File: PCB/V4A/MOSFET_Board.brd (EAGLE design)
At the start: 100 x 100 mm, 72 parts, among them IC101 7805T, Q101 IXTK102N65X2, Q102 BC817-16SMD, Q103 SIRC10DP, Q104 SIRC10DP, Q105 BC817-16SMD, Q106 BC807-16SMD, U101 AD620, U102 AD620, U103 LTC1865L, U104 LT1014I, U105 AD420, U106 LP2985-3.1, X201 SMKDSP_1,5/2, X202 SMKDSP_1,5/2

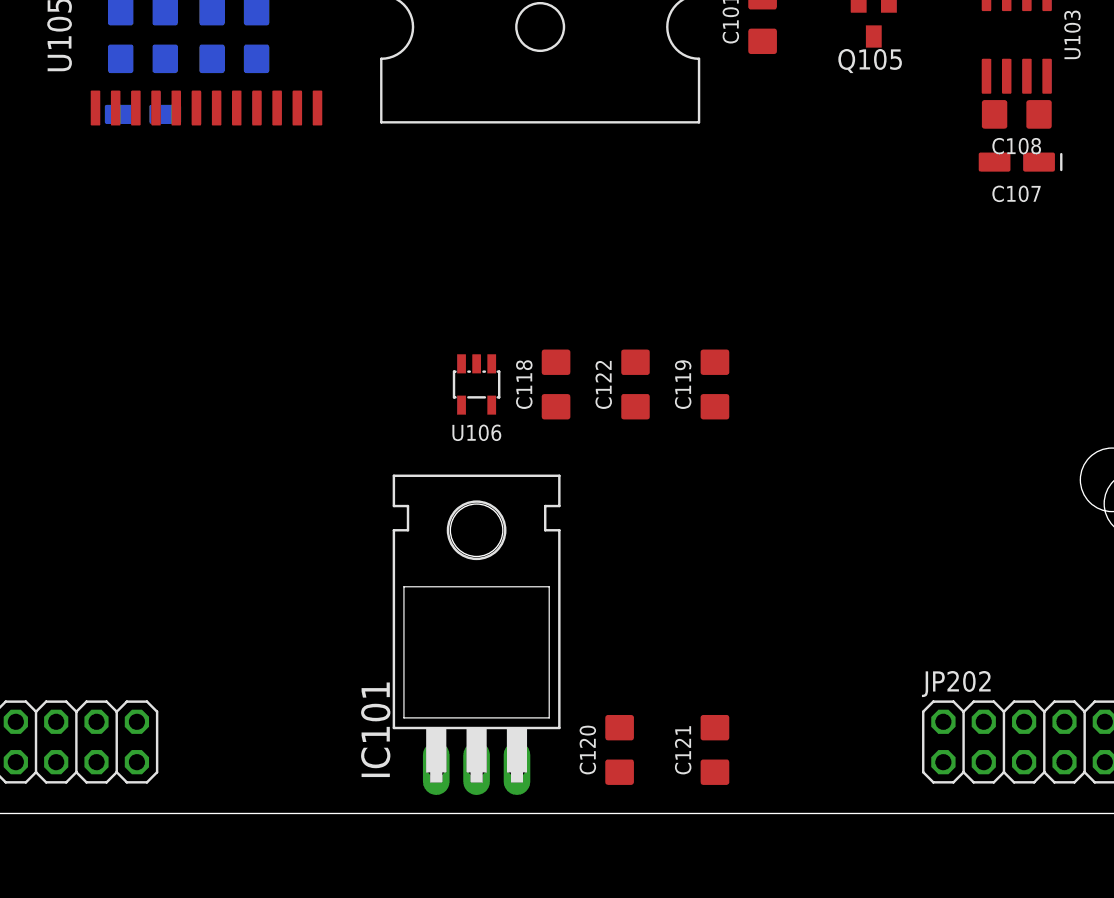
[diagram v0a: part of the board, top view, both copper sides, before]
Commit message: Added optoisolation to MOSFET board
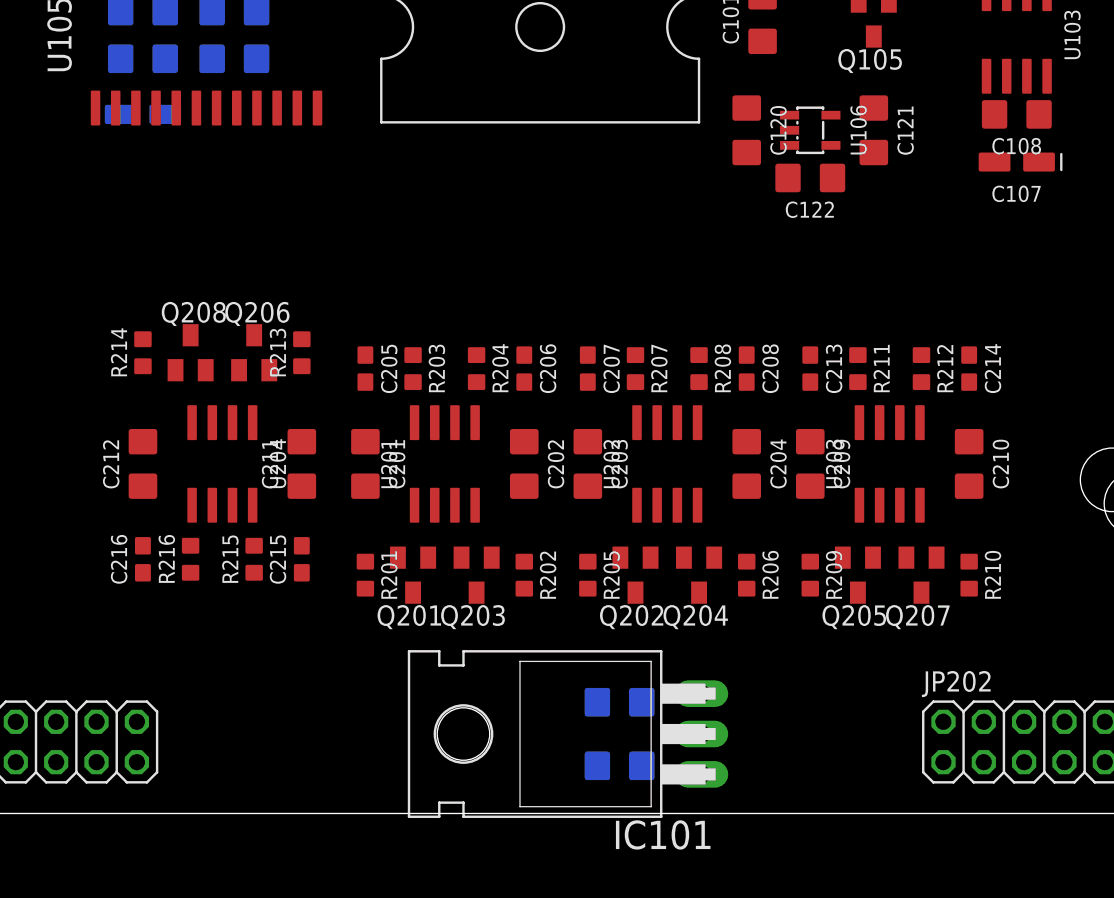
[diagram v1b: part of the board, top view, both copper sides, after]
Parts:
- added C201, C203, C209, C211: 0.1µ, passives:C3216
- added C202, C204, C210, C212: 0.01µ, passives:C3216
- added C205, C206, C207, C208, C213, C214, C215, C216: 15p, passives:C1608
- added Q201, Q202, Q203, Q204, Q205, Q206, Q207, Q208: BC807-16SMD, transistor-pnp:SOT23-BEC
- added R201, R202, R203, R204, R205, R206, R207, R208, R209, R210, R211, R212, R213, R214, R215, R216: 350R, passives:R1608
- added U201, U202, U203, U204: HCPL-063N, ic:SO8
- C118: value 1µ -> 0.33µ
- C119: value 2µ2 -> 0.1µ
- C120: value 0.33µ -> 1µ
- C121: value 0.1µ -> 2µ2
- moved C121 40.3 mm to (21.0, -14.0), turned to 270 degrees
- moved C120 39.8 mm to (13.0, -14.0), turned to 270 degrees
- moved U106 26.4 mm to (17.0, -14.0), turned to 270 degrees
- moved C118 24.3 mm to (5.00, -54.0), flipped to the bottom, turned to 0 degrees
- moved C119 20.9 mm to (5.00, -50.0), flipped to the bottom, turned to 0 degrees
- moved C122 17.0 mm to (17.0, -17.0), turned to 180 degrees
- moved IC101 8.94 mm to (0.00, -52.0), turned to 90 degrees
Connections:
- new net BYP_ISO: C102.1, C213.1, R106.1, R211.1, U203.7
- new net CLR_DAC_ISO: C205.1, R203.1, U105.6, U201.7
- new net FLT_DAC_ISO: Q208.B, U105.3
- new net MISO_ISO: Q206.B, U103.6
- new net MOSI_ISO: C208.1, R208.1, U103.5, U105.9, U202.6
- new net N$17: Q206.E, R213.1, U204.1
- new net N$18: Q208.E, R214.1, U204.4
- new net N$19: Q202.E, R205.1, U202.1
- new net N$20: Q204.E, R206.1, U202.4
- new net N$21: Q205.E, R209.1, U203.1
- new net N$22: Q207.E, R210.1, U203.4
- new net N$23: JP201.7
- new net N$24: JP201.5
- new net N$26: JP202.1
- new net N$27: JP201.9
- new net N$28: JP201.11
- new net N$29: JP201.13
- new net N$30: JP202.2
- new net N$32: JP201.6
- new net N$33: JP201.8
- new net N$34: JP201.10
- new net N$35: JP201.12
- new net N$36: JP201.14
- new net N$37: JP202.3
- new net N$38: JP202.5
- new net N$39: JP202.7
- new net N$40: JP202.9
- new net N$45: JP202.10
- new net N$46: JP202.8
- new net N$47: JP202.6
- new net N$48: JP202.4
- new net N$76: Q201.E, R201.1, U201.1
- new net N$77: Q203.E, R202.1, U201.4
- new net SCK_ISO: C207.1, R207.1, U103.7, U105.8, U202.7
- new net SS_C_ISO: C214.1, R212.1, U103.1, U203.6
- new net SS_DAC_ISO: C206.1, R204.1, U105.7, U201.6
- net +12V: now also C118.1, JP201.3, JP202.11; no longer C120.1
- net +15V: now also JP201.1, JP202.13
- net +3V3: now also C121.1, R207.2, R208.2, R212.2; no longer C119.1
- net +5V: now also C119.1, C201.1, C202.1, C203.1, C204.1, C209.1, C210.1, C211.1, C212.1, R201.2, R202.2, R203.2, R204.2, R205.2, R206.2, R209.2, R210.2, R211.2, R213.2, R214.2, R215.2, R216.2, U201.8, U202.8, U203.8, U204.8; no longer C121.1
- net -15V: now also JP201.2, JP202.14
- net BYP: now also Q205.B; no longer C102.1, R106.1
- net CLR_DAC: now also Q201.B; no longer U105.6
- net FLT_DAC: now also C216.1, R216.1, U204.6; no longer U105.3
- net GND: now also C201.2, C202.2, C203.2, C204.2, C205.2, C206.2, C207.2, C208.2, C209.2, C210.2, C211.2, C212.2, C213.2, C214.2, C215.2, C216.2, JP201.4, JP202.12, Q201.C, Q202.C, Q203.C, Q204.C, Q205.C, Q206.C, Q207.C, Q208.C, U201.2, U201.3, U201.5, U202.2, U202.3, U202.5, U203.2, U203.3, U203.5, U204.2, U204.3, U204.5
- net MISO: now also C215.1, R215.1, U204.7; no longer U103.6
- net MOSI: now also Q204.B; no longer U103.5, U105.9
- net SCK: now also Q202.B; no longer U103.7, U105.8
- net SS_C: now also Q207.B; no longer U103.1
- net SS_DAC: now also Q203.B; no longer U105.7
- net VREF: now also C120.1; no longer C118.1

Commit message: Changed to single board design
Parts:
- removed C201, C203, C209, C211: 0.1µ, passives:C3216
- removed C202, C204, C210, C212: 0.01µ, passives:C3216
- removed C205, C206, C207, C208, C213, C214, C215, C216: 15p, passives:C1608
- removed Q201, Q202, Q203, Q204, Q205, Q206, Q207, Q208: BC807-16SMD, transistor-pnp:SOT23-BEC
- removed R201, R202, R203, R204, R205, R206, R207, R208, R209, R210, R211, R212, R213, R214, R215, R216: 350R, passives:R1608
- removed U$2, U$3, U$4, U$5: (no value), mechanical:M3
- removed U201, U202, U203, U204: HCPL-063N, ic:SO8
- removed X201, X202: SMKDSP_1,5/2, con-phoenix-smkdsp:SMKDSP_1,5/2
- added C123, C124, C131, C132, C134, C301, C302, C309, C310: 0.1µ, passives:C3216
- added C125, C126, C127, C128: 100p, passives:C1608
- added C129, C130: 1µ, passives:CT3216
- added C133: 0.33µ, passives:C3216
- added C135: 1µ, passives:C3216
- added C136: 10n, passives:C3216
- added C137: 2µ2, passives:C3216
- added C303, C304, C311, C312: 0.01µ, passives:C3216
- added C305, C306, C307, C308, C313, C314, C315, C316: 15p, passives:C1608
- added D101, D102, D103, D104: BAT54S, diode:SOT23
- added HS102: (no value), mechanical:HEATSINK-LGA115X
- added LCD1: LCD-20X4, mechanical:4X20_LED
- added PS101: RFMM-0505S, modules:RECOM-SIP7
- added Q107, Q109: BC817, transistors:SOT23
- added Q108, Q110, Q301, Q302, Q303, Q304, Q305, Q306, Q307, Q308: BC807, transistors:SOT23
- added Q111, Q112: IXTK102N65X2, transistors:TO-264P-H-PADUP
- added R129, R130: 100R, passives:R3216W
- added R131, R133, R137, R139: 1k, passives:R1608
- added R132, R134, R138, R140, R143, R144: 2R, passives:R3216W
- added R135, R136: 100k, passives:R1608
- added R141, R142, R146, R148: 0R004, passives:R6332W
- added R145, R147, R149, R150, R151, R152: 2k15, passives:R2012W
- added R153, R154, R155, R156: 100R, passives:R2012W
- added R301, R302, R303, R304, R305, R306, R307, R308, R309, R310, R311, R312, R313, R314, R315, R316: 350R, passives:R1608
- added U$1: ARDUINO-MICRO, breakout:ARDUINO-MICRO
- added U107, U108: AD620, ic:SO8
- added U109, U110: LTC1865L, ic:SO8
- added U111: LP2985-3.1, ic:SOT23-5L
- added U301, U302, U303, U304: HCPL-063N, ic:SO8
- added X301, X302, X303, X304: SMKDSP_1,5/2, con-phoenix-smkdsp:SMKDSP_1,5/2
- C102: value 500p -> 0.1µ; device passives:C1608 -> passives:C3216
- C105, C106, C108: value 0.1µ -> 0.01µ
- C107: value 1µ -> 0.01µ; device passives:CT3216 -> passives:C3216
- C109, C110: value 500p -> 1µ; device passives:C1608 -> passives:CT3216
- C113, C114: value 0.01µ -> 0.1µ
- C115: value 1µ -> 0.1µ; device passives:CT3216 -> passives:C3216
- C118: value 0.33µ -> 0.1µ
- C120: value 1µ -> 0.1µ
- C121: value 2µ2 -> 0.1µ
- C122: value 10n -> 0.1µ
- HS101: value HEATSINK-LGA115X -> (none)
- Q101: value IXTK102N65X2 -> SIRC10DP; device transistors:TO-264P-H-PADUP -> transistors:POWERPAK-SO-8
- Q102, Q105: value BC817-16SMD -> SIRC10DP; device transistor-npn:SOT23-BEC -> transistors:POWERPAK-SO-8
- Q103, Q104: value SIRC10DP -> BC817; device transistors:POWERPAK-SO-8 -> transistors:SOT23
- Q106: value BC807-16SMD -> SIRC10DP; device transistor-pnp:SOT23-BEC -> transistors:POWERPAK-SO-8
- R101, R117: value 100k -> 10k
- R102: value 1k -> 10k
- R103, R104, R107: value 2R -> 10k; device passives:R3216W -> passives:R1608
- R105: value 2k15 -> 100k; device passives:R2012W -> passives:R1608
- R106: value 1k -> 100k
- R108, R109: value 0R004 -> 10k; device passives:R6332W -> passives:R1608
- R110, R111, R126: value 2k15 -> 10k; device passives:R2012W -> passives:R1608
- R112, R113: value 100R -> 10k; device passives:R2012W -> passives:R1608
- R123: value 100R -> 10k; device passives:R3216W -> passives:R1608
- R127, R128: value 10k -> 2k15; device passives:R1608 -> passives:R2012W
- U101, U102: value AD620 -> AD420; device ic:SO8 -> ic:SO24W
- U103: value LTC1865L -> LT1014I; device ic:SO8 -> ic:SO16W
- U105: value AD420 -> AD620; device ic:SO24W -> ic:SO8
- U106: value LP2985-3.1 -> AD620; device ic:SOT23-5L -> ic:SO8
- moved R108 342.6 mm to (-60.0, -304.0), turned to 0 degrees
- moved C120 330.0 mm to (-75.0, -332.0), turned to 0 degrees
- moved R110 329.1 mm to (-68.0, -304.0), turned to 0 degrees
- moved R104 323.5 mm to (-72.0, -304.0), turned to 0 degrees
- moved R112 320.4 mm to (-56.0, -304.0), turned to 0 degrees
- moved C104 317.5 mm to (-55.0, -293.0), turned to 0 degrees
- moved R106 316.9 mm to (-75.0, -299.0), turned to 0 degrees
- moved R124 312.8 mm to (-63.0, -299.0), flipped to the top, turned to 0 degrees
- moved R126 312.6 mm to (-67.0, -299.0), flipped to the top, turned to 0 degrees
- moved R120 312.0 mm to (-59.0, -299.0), flipped to the top, turned to 0 degrees
- moved C112 311.4 mm to (-70.0, -293.0), flipped to the top, turned to 0 degrees
- moved R118 311.4 mm to (-76.0, -304.0), flipped to the top, turned to 0 degrees
- moved C102 310.7 mm to (-60.0, -293.0), turned to 0 degrees
- moved R122 310.6 mm to (-71.0, -299.0), flipped to the top, turned to 0 degrees
- moved R117 310.0 mm to (-64.0, -304.0), flipped to the top, turned to 0 degrees
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- renumbered JP201 to JP301, JP202 to JP302
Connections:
- removed net BYP_GATE: Q102.E, Q106.E, R104.1, R105.2, R107.1
- removed net CSENSE_H: Q103.1, Q103.2, Q103.3, Q104.1, Q104.2, Q104.3, R103.1, R105.1, R108.2, R109.2, U101.3, U102.2
- removed net CSENSE_L: Q101.1, Q103.5, Q104.5, R103.2, R125.1, R126.1, U102.3
- removed net HIGHC: C109.1, R112.2, U103.2
- removed net LBQ12_G: Q103.4, R104.2
- removed net LBQ13_G: Q104.4, R107.2
- removed net LGATE: Q101.3, R123.2
- removed net LOWC: C110.1, R113.2, U103.3
- removed net SDO_DAC: U105.10
- new net +VI: PS101.1
- new net +VO: PS101.7
- new net -VI: PS101.2
- new net -VO: PS101.5
- new net 3.3V: U$1.19
- new net A: LCD1.15
- new net BPY1G1: Q101.4, R132.2
- new net BYP1: Q109.2, Q110.2, R132.1, R138.1, R147.1
- new net BYP1G2: Q105.4, R138.2
- new net BYP2: Q107.2, Q108.2, R134.1, R140.1, R145.2
- new net BYP2G1: Q102.4, R134.2
- new net BYP2G2: Q106.4, R140.2
- new net CLR_DAC1: U101.6
- new net CLR_DAC2: U102.6
- new net CONV_C1: U109.1
- new net CONV_C2: U110.1
- new net CSEN_H1: Q101.1, Q101.2, Q101.3, Q105.1, Q105.2, Q105.3, R141.2, R143.1, R146.2, R147.2, U105.3, U106.2
- new net CSEN_H2: Q102.1, Q102.2, Q102.3, Q106.1, Q106.2, Q106.3, R142.2, R144.1, R145.1, R148.2, U107.3, U108.2
- new net CSEN_L1: Q101.5, Q105.5, Q111.1, R101.1, R127.1, R143.2, U106.3
- new net CSEN_L2: Q102.5, Q106.5, Q112.1, R102.1, R128.1, R144.2, U108.3
- new net DAC_VOUT1: U102.17, U104.5
- new net HIGHC1: C125.1, R153.2, U109.2
- new net HIGHC2: C127.1, R155.2, U110.2
- new net K: LCD1.16
- new net LATCH_DAC: U101.7, U102.7
- new net LGATE_1: Q111.3, R129.2
- new net LGATE_2: Q112.3, R130.2
- new net LOWC1: C126.1, R154.2, U109.3
- new net LOWC2: C128.1, R156.2, U110.3
- new net N$15: U103.1, U103.2
- new net N$25: Q103.3, Q107.1, Q108.1, R137.1
- new net N$31: Q103.1, R131.2, R135.1
- new net N$41: C106.2, U102.21
- new net N$42: C108.2, U102.20
- new net N$43: R106.2, R108.2, R112.2, R116.1, R117.1, U104.6
- new net N$44: R118.2, R122.1, U104.10
- new net N$49: R102.2, R118.1, U104.11
- new net N$50: R104.2, R110.2, U104.12
- new net N$51: R122.2, R126.1, U104.15
- new net N$52: R126.2, R128.2, R130.1, U104.16
- new net N$53: R120.2, R124.2, U104.14
- new net N$54: R116.2, R117.2, R120.1, U104.7
- new net N$56: D103.3, R155.1, U107.6
- new net N$57: D104.3, R156.1, U108.6
- new net RG1_L1: R151.2, U107.1
- new net RG1_L2: R152.2, U108.1
- new net RG2_L1: R151.1, U107.8
- new net RG2_L2: R152.1, U108.8
- new net SDO_DAC1: U101.10, U102.9
- new net SDO_DAC2: U102.10
- new net VDD: LCD1.2
- new net VEE: LCD1.3
- new net VIN: U$1.32
- new net VSS: LCD1.1
- net +12V: now also C105.1, C106.1, C107.1, C108.1, C115.1, C116.1, C133.1, Q107.3, Q109.3, R135.2, R136.2, R137.2, R139.2, U101.23, U102.23; no longer C101.1, C117.1, C118.1, Q102.C, R101.2, R102.2, U105.23
- net +15V: now also C101.1, C102.1, C117.1, C118.1, C119.1, C120.1, U103.4, U105.7, U106.7, U107.7, U108.7; no longer C103.1, C105.1, C111.1, U101.7, U102.7
- net +3V3: now also C129.+, C130.+, C131.1, C132.1, C137.1, D101.2, D102.2, D103.2, D104.2, R308.2, R313.2, R314.2, U109.8, U110.8, U111.5; no longer C107.+, C108.1, C121.1, R207.2, R208.2, R212.2, U103.8, U106.5
- net +5V: now also C109.+, C110.+, C111.1, C112.1, C134.1, C301.1, C302.1, C303.1, C304.1, C309.1, C310.1, C311.1, C312.1, R301.2, R302.2, R303.2, R304.2, R305.2, R306.2, R307.2, R309.2, R310.2, R311.2, R312.2, R315.2, R316.2, U$1.29, U101.2, U102.2, U301.8, U302.8, U303.8, U304.8; no longer C115.+, C116.1, C119.1, C201.1, C202.1, C203.1, C204.1, C209.1, C210.1, C211.1, C212.1, R201.2, R202.2, R203.2, R204.2, R205.2, R206.2, R209.2, R210.2, R211.2, R213.2, R214.2, R215.2, R216.2, U105.2, U201.8, U202.8, U203.8, U204.8
- net -15V: now also C103.1, C121.1, C122.1, C123.1, C124.1, U103.13, U105.4, U106.4, U107.4, U108.4; no longer C106.1, C112.1, U101.4, U102.4
- net BYP: now also Q302.1; no longer Q205.B
- net BYP_ISO: now also C306.1, R131.1, R133.1, R306.1, U302.7; no longer C102.1, C213.1, R106.1, R211.1, U203.7
- net CLR_DAC: now also Q301.1; no longer Q201.B
- net CLR_DAC_ISO: now also C305.1, R305.1, U301.7; no longer C205.1, R203.1, U105.6, U201.7
- net DAC_VOUT: now also U101.17, U103.5; no longer U104.5, U105.17
- net DUT+: now also Q111.2, Q112.2, X301.1, X301.2; no longer Q101.2, X201.1, X201.2
- net DUT-: now also U105.2, U107.2; no longer U101.2
- net FLT_DAC: now also C316.1, R316.1, U101.3, U102.3, U304.6; no longer C216.1, R216.1, U204.6
- net FLT_DAC_ISO: now also Q308.1; no longer Q208.B, U105.3
- net GND: now also C102.2, C109.-, C110.-, C113.2, C114.2, C115.2, C123.2, C124.2, C125.2, C126.2, C127.2, C128.2, C129.-, C130.-, C131.2, C132.2, C133.2, C134.2, C135.2, C136.2, C137.2, C301.2, C302.2, C303.2, C304.2, C305.2, C306.2, C307.2, C308.2, C309.2, C310.2, C311.2, C312.2, C313.2, C314.2, C315.2, C316.2, D101.1, D102.1, D103.1, D104.1, Q103.2, Q104.2, Q108.3, Q110.3, Q301.3, Q302.3, Q303.3, Q304.3, Q305.3, Q306.3, Q307.3, Q308.3, R103.1, R104.1, R107.1, R110.1, R111.1, R112.1, R123.1, R124.1, R141.1, R142.1, R146.1, R148.1, U$1.31, U$1.6, U101.11, U101.4, U102.11, U102.4, U103.3, U106.5, U107.5, U108.5, U109.4, U110.4, U111.2, U301.2, U301.3, U301.5, U302.2, U302.3, U302.5, U303.2, U303.3, U303.5, U304.2, U304.3, U304.5, X302.1, X302.2; no longer C105.2, C106.2, C107.-, C108.2, C109.2, C110.2, C115.-, C201.2, C202.2, C203.2, C204.2, C205.2, C206.2, C207.2, C208.2, C209.2, C210.2, C211.2, C212.2, C213.2, C214.2, C215.2, C216.2, Q105.E, Q106.C, Q201.C, Q202.C, Q203.C, Q204.C, Q205.C, Q206.C, Q207.C, Q208.C, R118.1, R119.1, R122.1, R127.1, R128.1, U103.4, U105.11, U105.4, U106.2, U201.2, U201.3, U201.5, U202.2, U202.3, U202.5, U203.2, U203.3, U203.5, U204.2, U204.3, U204.5, X202.1, X202.2
- net MISO: now also C315.1, R315.1, U109.6, U110.6, U304.7; no longer C215.1, R215.1, U204.7
- net MISO_ISO: now also Q307.1; no longer Q206.B, U103.6
- net MOSI: now also Q306.1, U101.9, U109.5, U110.5; no longer Q204.B
- net MOSI_ISO: now also C314.1, R314.1, U303.6; no longer C208.1, R208.1, U103.5, U105.9, U202.6
- net N$1: now also R103.2, R109.2, U103.12; no longer R122.2, R127.2, U104.12
- net N$10: now also C136.1, U111.4; no longer C122.1, U106.4
- net N$11: now also R113.2, R119.1, U103.7; no longer R115.2, R116.1, U104.7
- net N$12: now also R105.2, R107.2, R111.2, R113.1, U103.6; no longer R115.1, R117.2, R118.2, R119.2, U104.6
- net N$13: now also R115.2, R121.1, U103.10; no longer R121.2, R124.1, U104.10
- net N$14: now also R101.2, R115.1, U103.11; no longer R121.1, R125.2, U104.11
- net N$16: now also D102.3, R154.1, U106.6; no longer R113.1, U102.6
- net N$17: now also Q307.2, R311.1, U304.1; no longer Q206.E, R213.1, U204.1
- net N$18: now also Q308.2, R312.1, U304.4; no longer Q208.E, R214.1, U204.4
- net N$19: now also Q305.2, R309.1, U303.1; no longer Q202.E, R205.1, U202.1
- net N$2: now also R121.2, R125.1, U103.15; no longer R120.1, R124.2, U104.15
- net N$20: now also Q306.2, R310.1, U303.4; no longer Q204.E, R206.1, U202.4
- net N$21: now also Q302.2, R302.1, U302.1; no longer Q205.E, R209.1, U203.1
- net N$22: now also Q304.2, R304.1, U302.4; no longer Q207.E, R210.1, U203.4
- net N$3: now also C105.2, U101.21; no longer C113.2, U105.21
- net N$4: now also C107.2, U101.20; no longer C114.2, U105.20
- net N$5: now also Q104.3, Q109.1, Q110.1, R139.1; no longer Q102.B, Q105.C, Q106.B, R102.1
- net N$6: now also R125.2, R127.2, R129.1, U103.16; no longer R120.2, R123.1, R126.2, U104.16
- net N$7: now also D101.3, R153.1, U105.6; no longer R112.1, U101.6
- net N$76: now also Q301.2, R301.1, U301.1; no longer Q201.E, R201.1, U201.1
- net N$77: now also Q303.2, R303.1, U301.4; no longer Q203.E, R202.1, U201.4
- net N$8: now also Q104.1, R133.2, R136.1; no longer C102.2, Q105.B, R101.1, R106.2
- net N$9: now also R119.2, R123.2, U103.14; no longer R116.2, R128.2, U104.14
- net RG1_L3: now also R149.2, U105.1; no longer R110.2, U101.1
- net RG1_L4: now also R150.2, U106.1; no longer R111.2, U102.1
- net RG2_L3: now also R149.1, U105.8; no longer R110.1, U101.8
- net RG2_L4: now also R150.1, U106.8; no longer R111.1, U102.8
- net SCK: now also Q305.1, U101.8, U102.8, U109.7, U110.7; no longer Q202.B
- net SCK_ISO: now also C313.1, R313.1, U303.7; no longer C207.1, R207.1, U103.7, U105.8, U202.7
- net SS_C: now also Q304.1; no longer Q207.B
- net SS_C_ISO: now also C308.1, R308.1, U302.6; no longer C214.1, R212.1, U103.1, U203.6
- net SS_DAC: now also Q303.1; no longer Q203.B
- net SS_DAC_ISO: now also C307.1, R307.1, U301.6; no longer C206.1, R204.1, U105.7, U201.6
- net VREF: now also C135.1, R105.1, R106.1, U101.14, U101.15, U102.15, U111.1, U111.3; no longer C120.1, R117.1, U105.14, U105.15, U106.1, U106.3
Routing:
- net N$55: track 1.27 -> 0.00 mm
- net N$15: track 0.00 -> 1.27 mm
- added copper zone on layer 1, net CSEN_H1
- added copper zone on layer 1, net CSEN_L2
- removed copper zone on layer 1, net CSENSE_H
- removed copper zone on layer 1, net CSENSE_L
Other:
- board size 100 x 100 mm -> 200 x 155 mm

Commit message: PCB layout
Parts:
- removed C133: 0.33µ, passives:C3216
- removed C134: 0.1µ, passives:C3216
- removed IC101: 7805T, linear:TO220H
- removed JP301, JP302: (no value), pinhead:2X07
- removed LCD1: LCD-20X4, mechanical:4X20_LED
- removed U$1: ARDUINO-MICRO, breakout:ARDUINO-MICRO
- removed X301, X302, X303, X304: SMKDSP_1,5/2, con-phoenix-smkdsp:SMKDSP_1,5/2
- added C1, C11, C220, C3, C6: 1µ, passives:CT3216
- added C10: 10µ, passives:CT6032
- added C12, C8: 10n, passives:C3216
- added C13: 22µ, passives:CT6032
- added C14, C15: 220µ, rcl:E3,5-10
- added C16, C18: 0.33µ, passives:C3216
- added C17, C19: 0.1µ, passives:C1608
- added C2, C215, C219, C221, C7, C9: 0.1µ, passives:C3216
- added C218, C4, C5: 500p, passives:C1608
- added D301, D302: 1N5817-B, diode:DO41-7.6
- added IC1, IC2: 7805T, linear:TO220H
- added J1: (no value), con-jack:SPC4078
- added JP1: (no value), pinhead:1X16
- added L301, L302: 100µ, passives:SRN1060
- added MOV201, MOV202, MOV203, MOV204: 180V, passives:R3225W
- added R1, R2: 0R01, passives:R6332W
- added R205, R206, R207, R212, R213: 2M, passives:R3216W
- added R214, R215: 2k15, passives:R2012W
- added R216, R3, R4: 100R, passives:R2012W
- added R217: 10k, passives:R1608
- added U$2, U$3: FAN_MOLEX4PIN, mechanical:MOLEX_47053-1000
- added U$6, U$7, U$8, U$9: (no value), mechanical:M4
- added U1, U2: LM50, ic:SOT23W
- added U205: AD620, ic:SO8
- added U208, U3: LTC1865L, ic:SO8
- added U4: MAX743, ic:SO16W
- added X1: GMSTBA4, con-phoenix-762:GMSTBA4
- C101, C102, C103, C104, C111, C112, C113, C114, C115, C116, C117, C118, C119, C120, C121, C122, C123, C124, C131, C132, C301, C302, C309, C310: device passives:C3216 -> passives:C1608
- C105, C107, C136: device passives:C3216 -> passives:C2012
- C137: value 2µ2 -> 4µ7
- R141, R142, R146, R148: value 0R004 -> 0R01
- R143, R144: value 2R -> 3R3
- moved R118 468.5 mm to (163.0, 99.0), turned to 270 degrees
- moved R104 467.0 mm to (169.0, 96.0), turned to 270 degrees
- moved R106 466.8 mm to (169.0, 99.0), turned to 270 degrees
- moved R110 463.4 mm to (166.0, 96.0), turned to 270 degrees
- moved R112 460.1 mm to (166.0, 99.0), turned to 270 degrees
- moved R117 459.9 mm to (163.0, 96.0), turned to 270 degrees
- moved R126 458.2 mm to (160.0, 99.0), turned to 270 degrees
- moved R108 456.8 mm to (166.0, 93.0), turned to 270 degrees
- moved R122 455.0 mm to (160.0, 93.0), turned to 270 degrees
- moved R124 453.6 mm to (160.0, 96.0), turned to 270 degrees
- moved R102 449.5 mm to (169.0, 93.0), turned to 270 degrees
- moved R116 448.5 mm to (163.0, 93.0), turned to 270 degrees
- moved R120 447.6 mm to (157.0, 93.0), turned to 270 degrees
- moved R130 445.9 mm to (170.0, 104.0), turned to 90 degrees
- moved U104 445.7 mm to (163.0, 96.0), flipped to the bottom
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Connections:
- removed net +VI: PS101.1
- removed net +VO: PS101.7
- removed net -VI: PS101.2
- removed net -VO: PS101.5
- removed net 3.3V: U$1.19
- removed net A: LCD1.15
- removed net K: LCD1.16
- removed net N$40: JP302.9
- removed net N$46: JP302.8
- removed net N$47: JP302.6
- removed net N$48: JP302.4
- removed net VDD: LCD1.2
- removed net VEE: LCD1.3
- removed net VIN: U$1.32
- removed net VREF: C135.1, R105.1, R106.1, U101.14, U101.15, U102.15, U111.1, U111.3
- removed net VSS: LCD1.1
- new net +5V_I: C310.1, C312.1, PS101.7
- new net FAN1_PWM: U$2.4
- new net FAN1_SIG: U$2.3
- new net FAN2_PWM: U$3.4
- new net FAN2_SIG: U$3.3
- new net GNDI: C310.2, C312.2, C315.2, C316.2, PS101.5, Q301.3, Q302.3, Q303.3, Q304.3, Q305.3, Q306.3, U301.2, U301.3, U302.2, U302.3, U303.2, U303.3, U304.5
- new net MISO_I: U208.6, U3.6
- new net MOSI_I: U208.5, U3.5
- new net RG1_H6: R215.2, U205.1
- new net RG2_H6: R215.1, U205.8
- new net SCK_I: U208.7, U3.7
- new net SS_TEMP_I: U3.1
- new net SS_V_I: U208.1
- new net T1_OUT: C1.+, R3.1, U1.2
- new net T2_OUT: C3.+, R4.1, U2.2
- new net TEMP1: C4.1, R3.2, U3.2
- new net TEMP2: C5.1, R4.2, U3.3
- new net VREF1: C135.1, R105.1, U101.14, U101.15, U111.1, U111.3
- new net VREF2: C10.+, R106.1, U102.14, U102.15, U4.6
- new net VSENSE+: MOV201.1, R205.1, X1.1
- new net VSENSE-: MOV204.2, U205.2, X1.4
- net +12V: now also C16.1, C18.1, IC1.1, IC2.1, J1.3, U$2.2, U$3.2; no longer C133.1, IC101.1, JP301.3, JP302.11
- net +15V: now also C14.+, C215.1, D301.C, U205.7, U4.16; no longer JP301.1, JP302.13
- net +3V3: now also C220.+, C221.1, C6.+, C7.1, U208.8, U3.8
- net +5V: now also C13.+, C17.1, C19.1, C2.1, C9.2, IC1.3, IC2.3, L302.1, PS101.1, U1.1, U2.1, U4.12, U4.13, U4.3, U4.4, U4.5; no longer C134.1, C310.1, C312.1, IC101.3, U$1.29
- net -15V: now also C15.-, C219.1, D302.A, U205.4, U4.9; no longer JP301.2, JP302.14
- net CSEN_H1: now also R1.2
- net CSEN_H2: now also R2.2
- net DUT+: now also X1.2; no longer X301.1, X301.2
- net DUT-: now also R1.1, R103.1, R104.1, R141.1, R142.1, R146.1, R148.1, R2.1, X1.3
- net GND: now also C1.-, C10.-, C11.-, C12.2, C13.-, C14.-, C15.+, C16.2, C17.2, C18.2, C19.2, C2.2, C215.2, C218.2, C219.2, C220.-, C221.2, C3.-, C4.2, C5.2, C6.-, C7.2, C8.1, C9.1, IC1.2, IC2.2, J1.1, L301.2, PS101.2, R214.1, R217.1, U$2.1, U$3.1, U1.3, U2.3, U205.5, U208.4, U3.4, U4.11, U4.14, U4.2; no longer C133.2, C134.2, C310.2, C312.2, C315.2, C316.2, IC101.2, JP301.4, JP302.12, Q301.3, Q302.3, Q303.3, Q304.3, Q305.3, Q306.3, R103.1, R104.1, R141.1, R142.1, R146.1, R148.1, U$1.31, U$1.6, U301.2, U301.3, U302.2, U302.3, U303.2, U303.3, U304.5, X302.1, X302.2
- net N$23: now also R216.1, U205.6; no longer JP301.7
- net N$24: now also R212.1, R213.2; no longer JP301.5
- net N$26: now also R206.2, R212.2; no longer JP302.1
- net N$27: now also R206.1, R207.2; no longer JP301.9
- net N$28: now also MOV201.2, MOV202.1; no longer JP301.11
- net N$29: now also R213.1, R214.2, U205.3; no longer JP301.13
- net N$30: now also C218.1, R216.2, U208.2; no longer JP302.2
- net N$32: now also MOV202.2, MOV203.1; no longer JP301.6
- net N$33: now also R205.2, R207.1; no longer JP301.8
- net N$34: now also C12.1, U4.8; no longer JP301.10
- net N$35: now also C11.+, U4.7; no longer JP301.12
- net N$36: now also MOV203.2, MOV204.1; no longer JP301.14
- net N$37: now also C8.2, U4.1; no longer JP302.3
- net N$38: now also D301.A, L302.2, U4.15; no longer JP302.5
- net N$39: now also D302.C, L301.1, U4.10; no longer JP302.7
- net N$45: now also R217.2, U208.3; no longer JP302.10
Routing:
- net GND: track 3.00 -> 84.9 mm, vias 0 -> 16
- net CSEN_L1: track 0.00 -> 36.8 mm
- net CSEN_H1: track 0.00 -> 32.3 mm
- net +12V: track 0.00 -> 25.3 mm, vias 0 -> 1
- net HIGHC1: track 0.00 -> 22.6 mm
- net N$13: track 0.00 -> 22.1 mm
- net +3V3: track 0.00 -> 21.6 mm, vias 0 -> 2
- net N$14: track 0.00 -> 19.6 mm
- net -15V: track 0.00 -> 17.8 mm, vias 0 -> 4
- net DUT-: track 0.00 -> 17.3 mm
- net N$5: track 0.00 -> 13.9 mm
- net N$12: track 0.00 -> 13.5 mm
- net BPY1G1: track 0.00 -> 13.5 mm, vias 0 -> 2
- net VREF1: track 0.00 -> 12.6 mm
- net DAC_VOUT: track 0.00 -> 12.3 mm
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- added copper zone on layer 16, net CSEN_H1
- added copper zone on layer 16, net CSEN_H2
- added copper zone on layer 16, net CSEN_L1
- added copper zone on layer 16, net CSEN_L2
- added copper zone on layer 16, net DUT-
- added copper zone on layer 15, net GND
- added copper zone on layer 15, net GNDI
- removed copper zone on layer 1, net CSEN_H1
- removed copper zone on layer 1, net CSEN_L2
- removed copper zone on layer 1, net GND
- removed copper zone on layer 2, net GND
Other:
- board size 200 x 155 mm -> 230 x 120 mm
